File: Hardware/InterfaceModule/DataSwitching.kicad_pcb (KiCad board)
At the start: 2 copper layers, 76 x 76 mm, 14 parts, among them J11 TS-480 DATA, J12 D-700 DATA, J13 SignaLink 2 RADIO, J14 SignaLink 1 RADIO, K10 FINDER-40.52, K11 FINDER-40.52, K12 FINDER-40.52, K13 FINDER-40.52, K14 FINDER-40.52, K9 FINDER-40.52

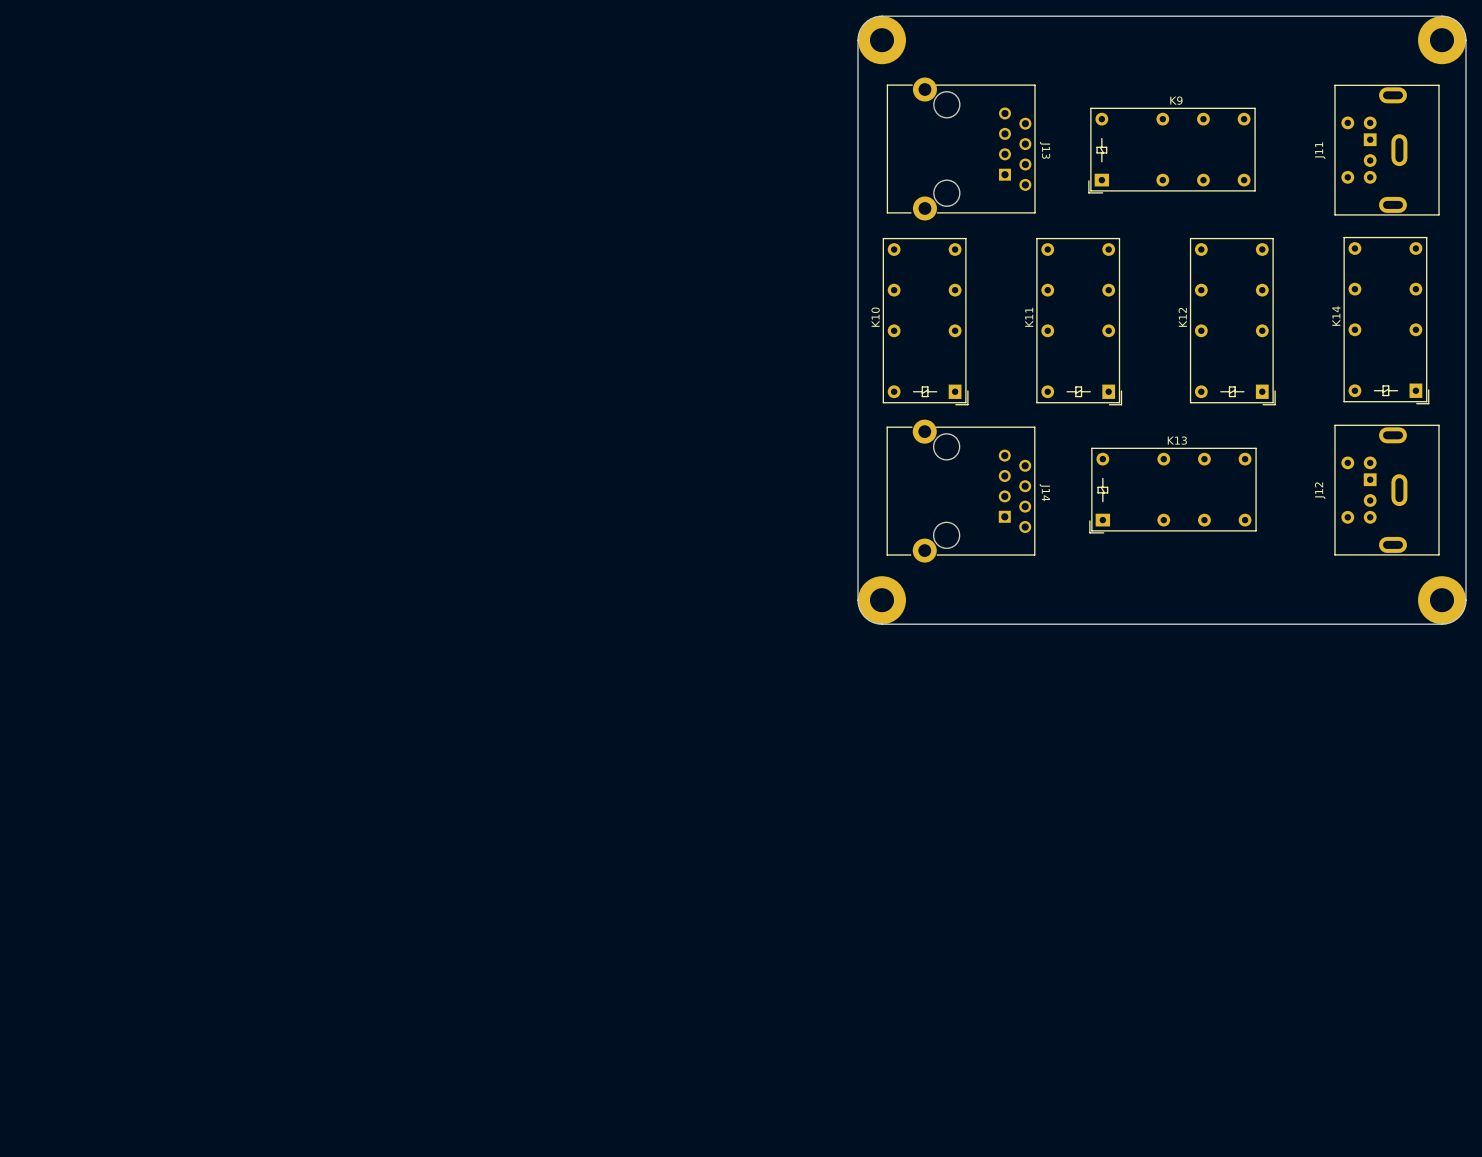
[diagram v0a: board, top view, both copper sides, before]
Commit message: Updated silkscreen dates, corrected gerber files
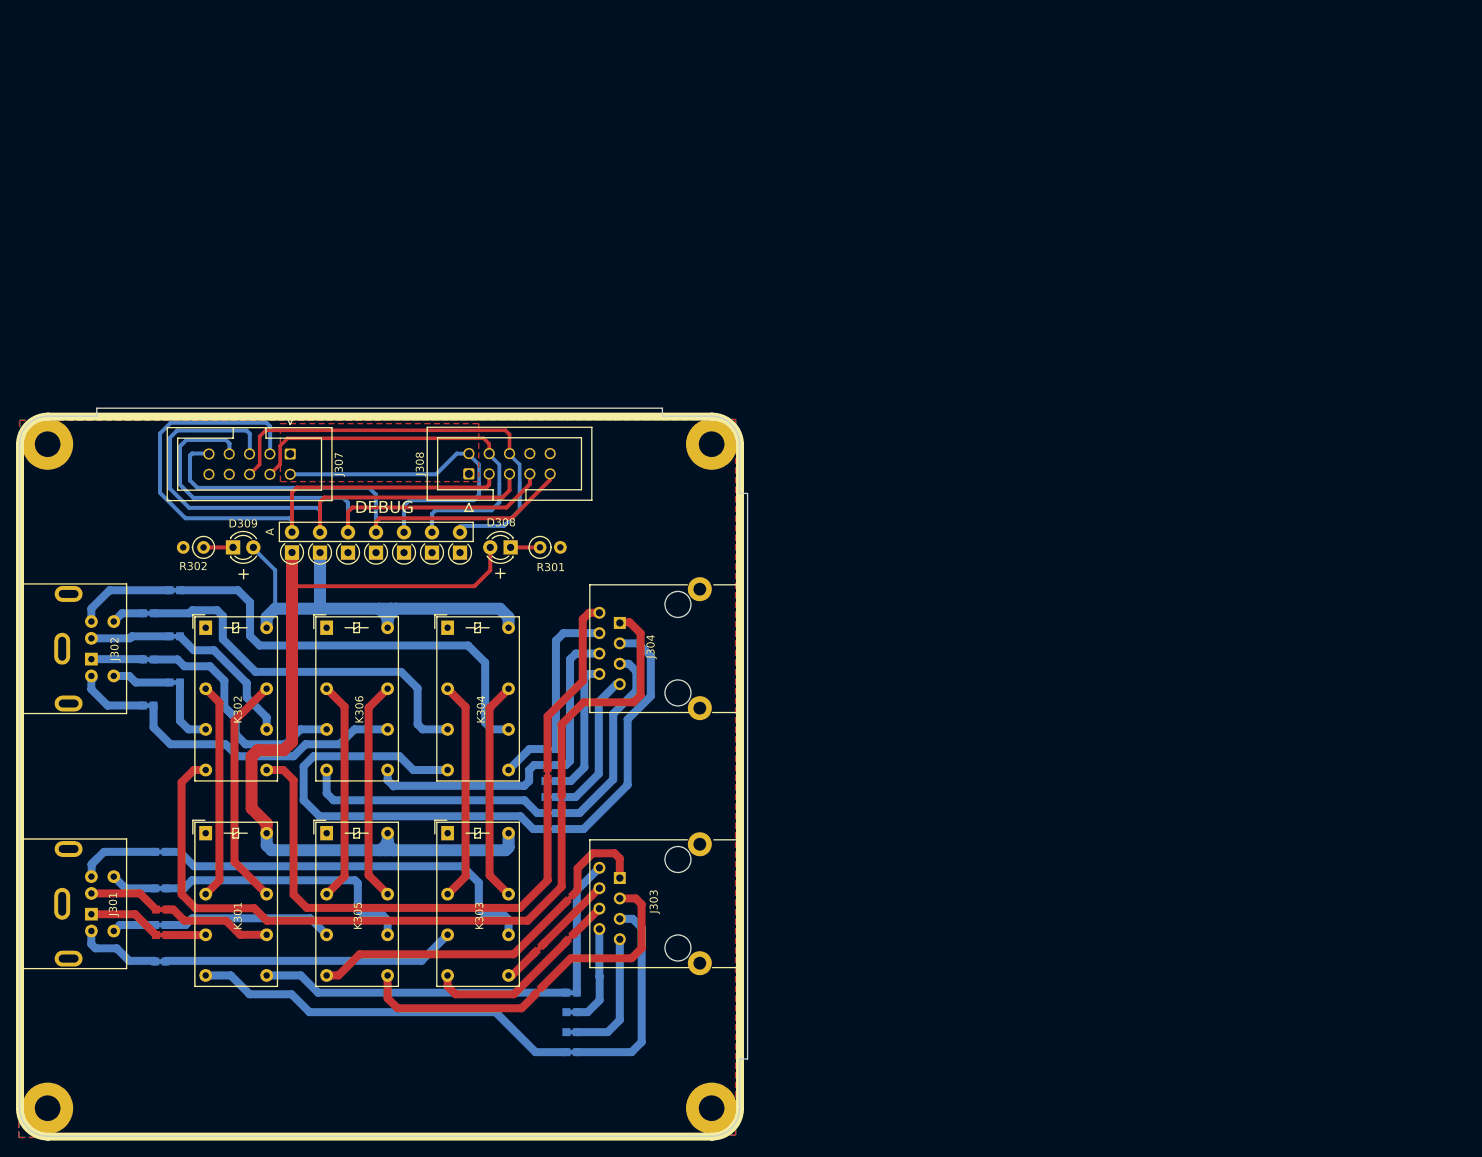
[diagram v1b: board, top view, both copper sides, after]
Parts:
- removed H1, H2, H3, H4: Mounting Hole, 
- removed J11: TS-480 DATA, libraries:Connector_Mini-DIN_Female_6Pin_2rows
- removed J12: D-700 DATA, libraries:Connector_Mini-DIN_Female_6Pin_2rows
- removed J13: SignaLink 2 RADIO, libraries:Mystery_RJ45
- removed J14: SignaLink 1 RADIO, libraries:Mystery_RJ45
- removed K10, K11, K12, K13, K14, K9: FINDER-40.52, Relay_THT:Relay_DPDT_Finder_30.22
- added D301: D_Small_Filled, Diode_THT:D_A-405_P2.54mm_Vertical_AnodeUp, F.Cu at (44.6, 124.5)
- added D302: D_Small_Filled, Diode_THT:D_A-405_P2.54mm_Vertical_AnodeUp, F.Cu at (48.1, 124.6)
- added D303: D_Small_Filled, Diode_THT:D_A-405_P2.54mm_Vertical_AnodeUp, F.Cu at (51.6, 124.6)
- added D304: D_Small_Filled, Diode_THT:D_A-405_P2.54mm_Vertical_AnodeUp, F.Cu at (55.1, 124.6)
- added D305: D_Small_Filled, Diode_THT:D_A-405_P2.54mm_Vertical_AnodeUp, F.Cu at (58.6, 124.6)
- added D306: D_Small_Filled, Diode_THT:D_A-405_P2.54mm_Vertical_AnodeUp, F.Cu at (62.1, 124.6)
- added D307: D_Small_Filled, Diode_THT:D_A-405_P2.54mm_Vertical_AnodeUp, F.Cu at (65.6, 124.6)
- added D308: LED, LED_THT:LED_D3.0mm, F.Cu at (71.9, 123.9)
- added D309: LED, LED_THT:LED_D3.0mm, F.Cu at (37.2, 123.9)
- added G***: LOGO, libraries:LogoSmallInvert, B.Cu at (40.0, 188.0)
- added H301: Mounting Hole, libraries:M3_Mounting, F.Cu at (97.0, 111.0)
- added H302: Mounting Hole, libraries:M3_Mounting, F.Cu at (97.0, 194.0)
- added H303: Mounting Hole, libraries:M3_Mounting, F.Cu at (14.0, 111.0)
- added H304: Mounting Hole, libraries:M3_Mounting, F.Cu at (14.0, 194.0)
- added J301: TS-480 DATA, libraries:Connector_Mini-DIN_Female_6Pin_2rows, F.Cu at (19.5, 169.8)
- added J302: D-700 DATA, libraries:Connector_Mini-DIN_Female_6Pin_2rows, F.Cu at (19.5, 137.9)
- added J303: SignaLink 2 RADIO, libraries:Mystery_RJ45, F.Cu at (85.5, 165.3)
- added J304: SignaLink 1 RADIO, libraries:Mystery_RJ45, F.Cu at (85.5, 133.4)
- added J307: 2x05 IDC Header - IN, Connector_IDC:IDC-Header_2x05_P2.54mm_Vertical, F.Cu at (44.3, 112.2)
- added J308: 2x05 IDC Header - OUT, Connector_IDC:IDC-Header_2x05_P2.54mm_Vertical, F.Cu at (66.7, 114.7)
- added JP301: Jumper_2_Bridged, libraries:1.0mm_Bridge, B.Cu at (28.1, 166.5)
- added JP302: Jumper_2_Bridged, libraries:1.0mm_Bridge, B.Cu at (28.1, 171.1)
- added JP303: Jumper_2_Bridged, libraries:1.0mm_Bridge, B.Cu at (26.6, 132.1)
- added JP304: Jumper_2_Bridged, libraries:1.0mm_Bridge, B.Cu at (29.9, 140.8)
- added JP305: Jumper_2_Bridged, libraries:1.0mm_Bridge, B.Cu at (28.1, 162.0)
- added JP306: Jumper_2_Bridged, libraries:1.0mm_Bridge, B.Cu at (28.1, 175.7)
- added JP307: Jumper_2_Bridged, libraries:1.0mm_Bridge, B.Cu at (29.9, 129.3)
- added JP308: Jumper_2_Bridged, libraries:1.0mm_Bridge, B.Cu at (26.6, 143.7)
- added JP309: Jumper_2_Bridged, libraries:1.0mm_Bridge, F.Cu at (28.2, 169.2)
- added JP310: Jumper_2_Bridged, libraries:1.0mm_Bridge, F.Cu at (28.2, 172.4)
- added JP311: Jumper_2_Bridged, libraries:1.0mm_Bridge, B.Cu at (29.9, 135.0)
- added JP312: Jumper_2_Bridged, libraries:1.0mm_Bridge, B.Cu at (26.6, 137.9)
- added JP313: Jumper_2_Bridged, libraries:1.0mm_Bridge, F.Cu at (79.3, 167.7)
- added JP314: Jumper_2_Bridged, libraries:1.0mm_Bridge, F.Cu at (78.3, 155.5)
- added JP315: Jumper_2_Bridged, libraries:1.0mm_Bridge, B.Cu at (79.5, 179.6)
- added JP316: Jumper_2_Bridged, libraries:1.0mm_Bridge, F.Cu at (76.5, 152.2)
- added JP317: Jumper_2_Bridged, libraries:1.0mm_Bridge, F.Cu at (75.4, 179.3)
- added JP318: Jumper_2_Bridged, libraries:1.0mm_Bridge, B.Cu at (76.9, 159.1)
- added JP319: Jumper_2_Bridged, libraries:1.0mm_Bridge, F.Cu at (75.4, 174.0)
- added JP320: Jumper_2_Bridged, libraries:1.0mm_Bridge, B.Cu at (76.9, 149.1)
- added JP321: Jumper_2_Bridged, libraries:1.0mm_Bridge, B.Cu at (79.5, 187.0)
- added JP322: Jumper_2_Bridged, libraries:1.0mm_Bridge, B.Cu at (76.9, 157.1)
- added JP323: Jumper_2_Bridged, libraries:1.0mm_Bridge, F.Cu at (79.3, 172.7)
- added JP324: Jumper_2_Bridged, libraries:1.0mm_Bridge, B.Cu at (76.9, 151.1)
- added JP325: Jumper_2_Bridged, libraries:1.0mm_Bridge, B.Cu at (79.5, 184.5)
- added JP326: Jumper_2_Bridged, libraries:1.0mm_Bridge, B.Cu at (76.9, 155.1)
- added JP327: Jumper_2_Bridged, libraries:1.0mm_Bridge, B.Cu at (79.5, 182.0)
- added JP328: Jumper_2_Bridged, libraries:1.0mm_Bridge, B.Cu at (76.9, 153.1)
- added K301: FINDER-40.52, Relay_THT:Relay_DPDT_Finder_30.22, F.Cu at (33.8, 159.6)
- added K302: FINDER-40.52, Relay_THT:Relay_DPDT_Finder_30.22, F.Cu at (33.8, 133.9)
- added K303: FINDER-40.52, Relay_THT:Relay_DPDT_Finder_30.22, F.Cu at (64.0, 159.6)
- added K304: FINDER-40.52, Relay_THT:Relay_DPDT_Finder_30.22, F.Cu at (64.0, 133.9)
- added K305: FINDER-40.52, Relay_THT:Relay_DPDT_Finder_30.22, F.Cu at (48.9, 159.6)
- added K306: FINDER-40.52, Relay_THT:Relay_DPDT_Finder_30.22, F.Cu at (48.9, 133.9)
- added R301: 680Ω, Resistor_THT:R_Axial_DIN0207_L6.3mm_D2.5mm_P2.54mm_Vertical, F.Cu at (75.6, 123.9)
- added R302: 680Ω, Resistor_THT:R_Axial_DIN0207_L6.3mm_D2.5mm_P2.54mm_Vertical, F.Cu at (33.5, 123.9)
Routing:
- net /Data Port Switching/Knob_Pos_1: track 0.00 -> 107.0 mm
- net /Data Port Switching/SignaLink1_RADIO_0: track 0.00 -> 78.5 mm
- net /Data Port Switching/Knob_Pos_1_Raw: track 0.00 -> 75.0 mm
- net /Data Port Switching/Knob_Pos_2_Raw: track 0.00 -> 70.4 mm
- net /Data Port Switching/Knob_Pos_3_Raw: track 0.00 -> 65.3 mm
- net /Data Port Switching/SignaLink1_RADIO_1: track 0.00 -> 64.8 mm
- net /Data Port Switching/Knob_Pos_4_Raw: track 0.00 -> 60.3 mm
- net /Data Port Switching/Knob_Pos_2: track 0.00 -> 55.5 mm
- net /Data Port Switching/SignaLink1_RADIO_2: track 0.00 -> 55.2 mm
- net /Data Port Switching/Knob_Pos_7_Raw: track 0.00 -> 55.2 mm
- net /Data Port Switching/D700_DATA_PR9: track 0.00 -> 55.1 mm
- net /Data Port Switching/480_DATA_NC: track 0.00 -> 50.2 mm
- net /Data Port Switching/Knob_Pos_6_Raw: track 0.00 -> 49.8 mm
- net /Data Port Switching/SignaLink2_RADIO_4: track 0.00 -> 49.1 mm
- net /Data Port Switching/D700_DATA_SQC: track 0.00 -> 47.4 mm
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- added copper zone on F.Cu, net +12P
- added copper zone on B.Cu, net GND
- added copper zone on F.Cu, net GND
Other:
- board size 76 x 76 mm -> 91 x 91 mm
- board text added: "+"
- board text added: "D-700 DATA"
- board text added: "DEBUG"
- board text added: "Data Module Rev 1. Thomas Francois Feb 27th, 2023"
- board text added: "IN"
- board text added: "OUT"
- board text added: "Signalink 1 RADIO"
- board text added: "Signalink 2 RADIO"
- board text added: "TS-480 DATA"
